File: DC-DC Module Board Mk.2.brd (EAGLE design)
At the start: 177.9 x 101.7 mm, 148 parts, among them U1 PCA9685, U3 LM1085IS-5.0

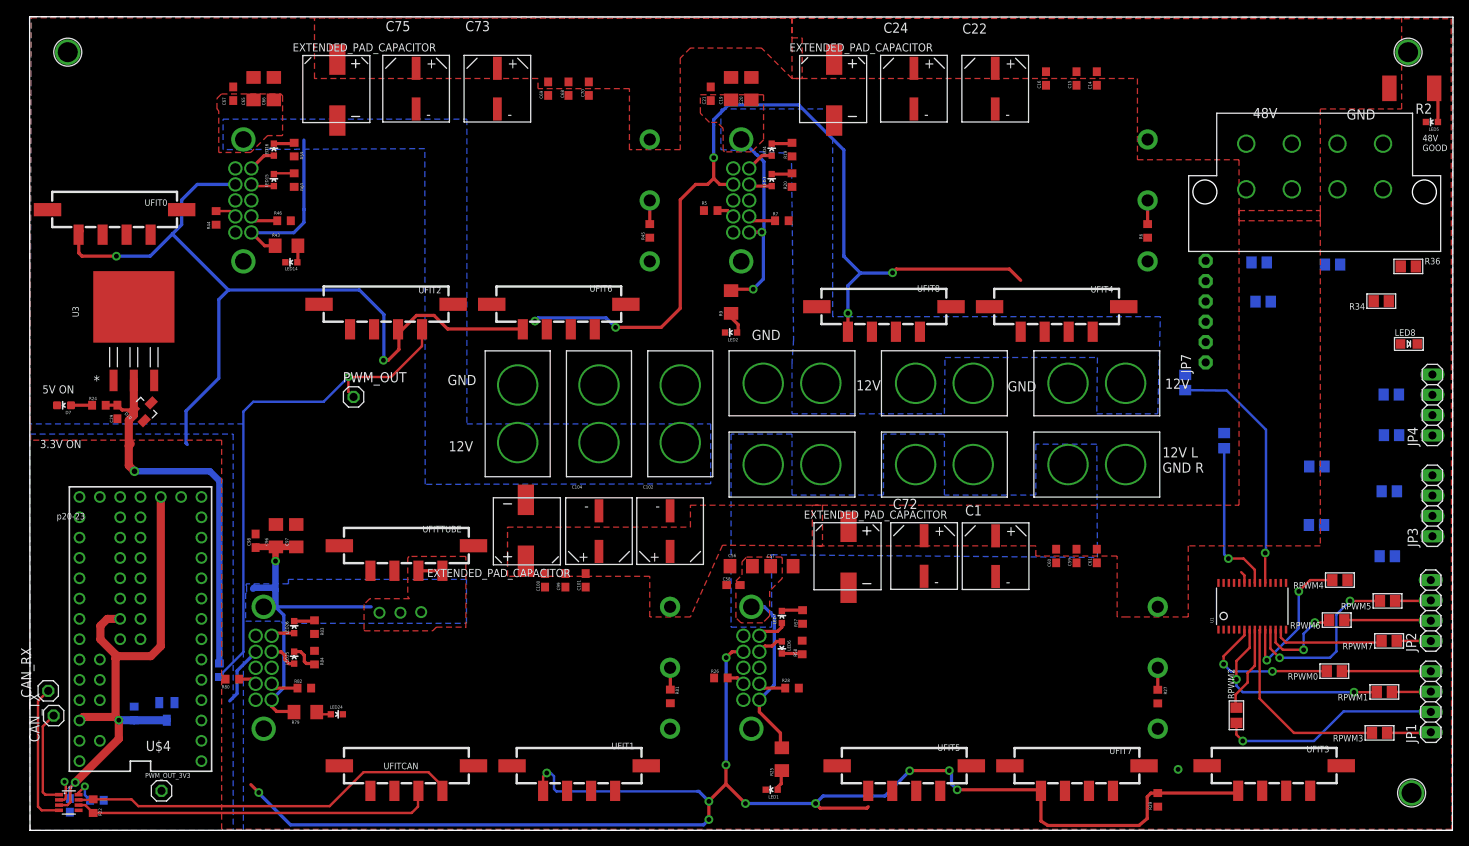
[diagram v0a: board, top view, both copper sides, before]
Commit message: pwm chip headers wired
need to give the bottom half more room so wires can come in
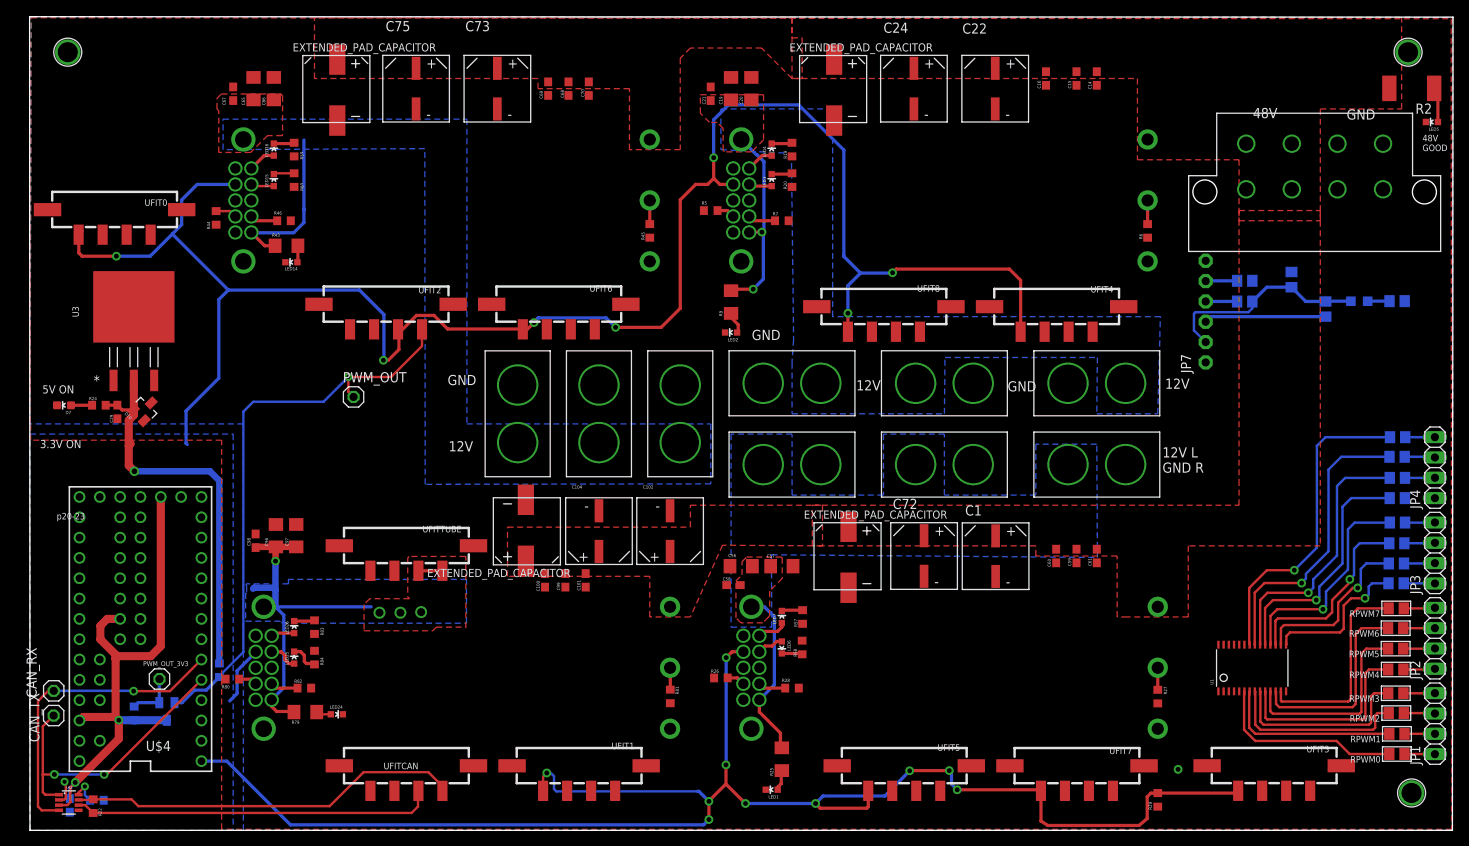
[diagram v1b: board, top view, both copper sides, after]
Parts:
- moved RPWM12 30.2 mm to (170.9, 40.3), turned to 0 degrees
- moved RPWM14 21.7 mm to (170.9, 45.4), turned to 0 degrees
- moved RPWM2 20.0 mm to (170.8, 13.4), turned to 180 degrees
- moved RPWM8 17.6 mm to (170.8, 29.6)
- moved PWM_OUT_3V3 14.0 mm to (16.2, 17.6)
- moved RPWM4 13.2 mm to (170.7, 18.8)
- moved RPWM0 13.0 mm to (170.9, 8.27)
- moved RPWM13 10.4 mm to (170.9, 42.8)
- moved RPWM10 10.3 mm to (170.8, 34.6)
- moved RPWM9 9.06 mm to (170.8, 32.1)
- moved LED8 8.18 mm to (166.2, 64.9), flipped to the bottom, turned to 90 degrees
- moved JP4 7.84 mm to (175.6, 44.1)
- moved U1 7.72 mm to (152.8, 19.0)
- moved RPWM6 7.44 mm to (170.7, 24.0)
- moved R34 7.06 mm to (161.9, 63.9), flipped to the bottom, turned to 90 degrees
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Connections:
- net DGND: now also UFIT4.C1, UFIT5.C1, UFIT6.C1
- net N$14: now also JP2.3; no longer JP2.2
- net N$20: now also JP2.4; no longer JP2.1
- net N$21: now also JP2.2; no longer JP2.3
- net N$24: now also JP2.1; no longer JP2.4
- net N$26: now also JP1.4; no longer JP1.1
- net N$27: now also JP1.3; no longer JP1.2
- net N$28: now also JP1.2; no longer JP1.3
- net N$29: now also JP1.1; no longer JP1.4
- net N$30: now also JP3.1; no longer JP3.4
- net N$31: now also JP3.2; no longer JP3.3
- net N$32: now also JP3.3; no longer JP3.2
- net N$37: now also JP3.4; no longer JP3.1
- net N$38: now also JP4.1; no longer JP4.4
- net N$39: now also JP4.2; no longer JP4.3
- net N$40: now also JP4.3; no longer JP4.2
- net N$41: now also JP4.4; no longer JP4.1
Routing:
- net PWM15: track 0.00 -> 40.0 mm, vias 0 -> 1
- net PWM13: track 0.00 -> 33.8 mm, vias 0 -> 1
- net PWM11: track 0.00 -> 27.4 mm, vias 0 -> 1
- net VCC: track 0.00 -> 26.4 mm
- net TXD: track 12.3 -> 37.0 mm, vias 0 -> 2
- net PWM10: track 0.00 -> 24.3 mm, vias 0 -> 1
- net N$27: track 27.7 -> 3.90 mm, vias 1 -> 0
- net PWM9: track 0.00 -> 21.4 mm, vias 0 -> 1
- net RXD: track 17.8 -> 38.6 mm, vias 0 -> 1
- net PWM8: track 0.00 -> 18.9 mm, vias 0 -> 1
- net DGND: track 424.3 -> 442.0 mm, vias 19 -> 18
- net PWM14: track 19.5 -> 36.7 mm
- net SDA: track 0.00 -> 15.2 mm
- net PWM6: track 11.4 -> 25.0 mm, vias 2 -> 0
- net PWM2: track 10.8 -> 22.9 mm
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
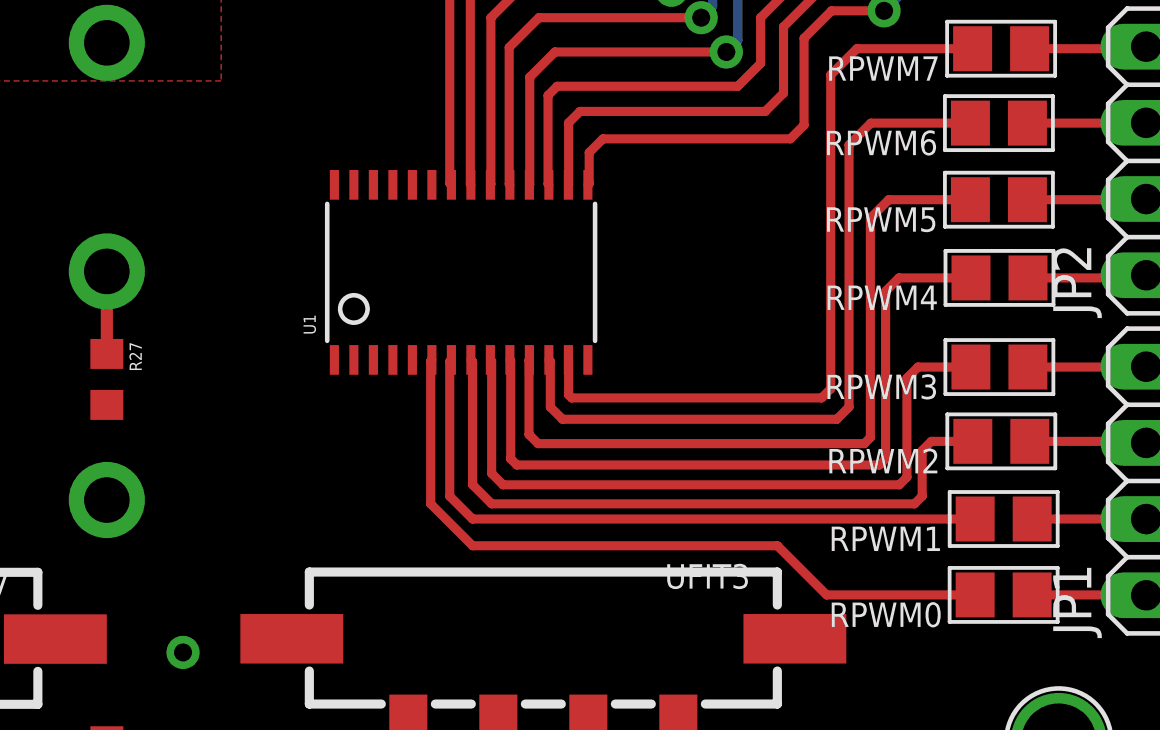
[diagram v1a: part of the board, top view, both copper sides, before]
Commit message: expanded space for other traces to reach pwm lines
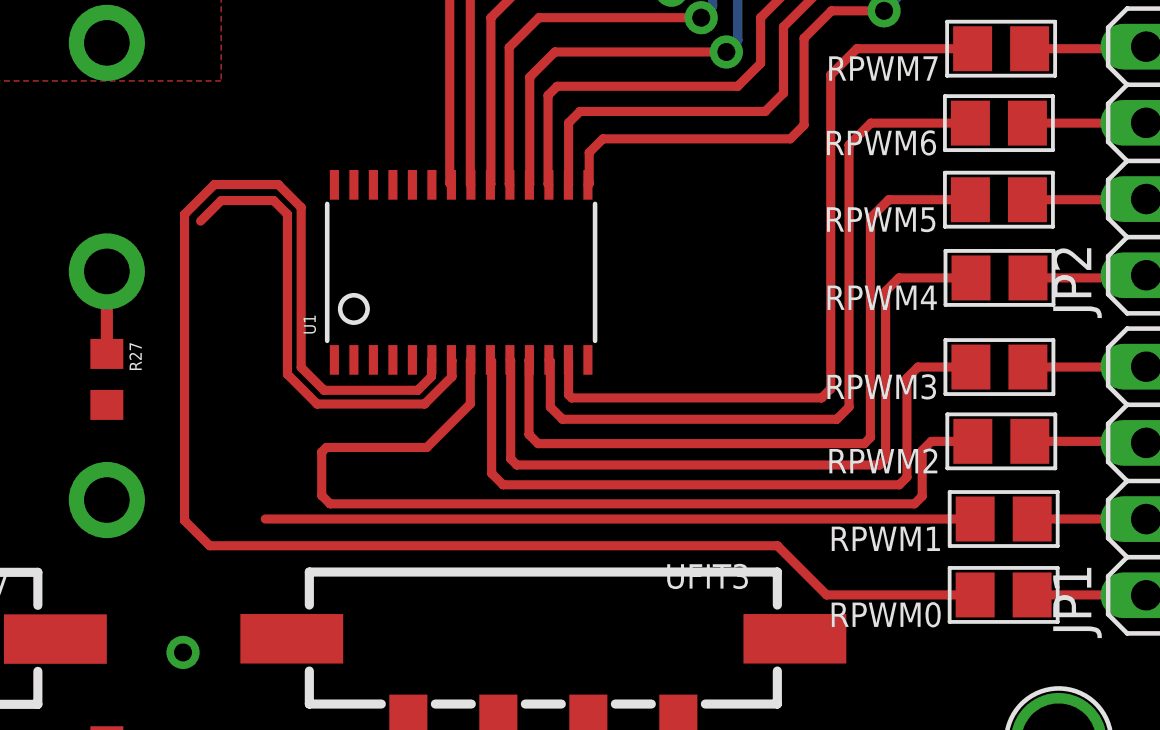
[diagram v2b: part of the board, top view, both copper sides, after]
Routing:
- net PWM0: track 24.2 -> 52.9 mm
- net PWM1: track 22.4 -> 39.2 mm
- net PWM2: track 22.9 -> 32.1 mm
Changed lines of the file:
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@@
 <contactref element="C22V4" pad="P$1"/>
 <wire x1="157.005" y1="16.1006" x2="150.505" y2="21.9362" width="0" layer="19" extent="1-1"/>
+<wire x1="140.97" y1="14.6" x2="150.505" y2="21.9362" width="0" layer="19" extent="1-1"/>
 </signal>
 <signal name="N$7">
@@
 <wire x1="169.9132" y1="8.2668" x2="164.9612" y2="8.2668" width="0.3048" layer="1"/>
 <wire x1="164.9612" y1="8.2668" x2="163.322" y2="9.906" width="0.3048" layer="1"/>
-<wire x1="163.322" y1="9.906" x2="153.162" y2="9.906" width="0.3048" layer="1"/>
-<wire x1="153.162" y1="9.906" x2="151.765" y2="11.303" width="0.3048" layer="1"/>
-<wire x1="151.765" y1="11.303" x2="151.765" y2="16.0606" width="0.3048" layer="1"/>
-<wire x1="151.765" y1="16.0606" x2="151.805" y2="16.1006" width="0.3048" layer="1"/>
+<wire x1="163.322" y1="9.906" x2="144.399" y2="9.906" width="0.3048" layer="1"/>
+<wire x1="144.399" y1="9.906" x2="143.5608" y2="10.7442" width="0.3048" layer="1"/>
+<wire x1="151.7904" y1="16.086" x2="151.805" y2="16.1006" width="0.3048" layer="1"/>
+<wire x1="143.5608" y1="10.7442" x2="143.5608" y2="20.955" width="0.3048" layer="1"/>
+<wire x1="143.5608" y1="20.955" x2="144.5514" y2="21.9456" width="0.3048" layer="1"/>
+<wire x1="144.5514" y1="21.9456" x2="146.685" y2="21.9456" width="0.3048" layer="1"/>
+<wire x1="146.685" y1="21.9456" x2="147.447" y2="21.1836" width="0.3048" layer="1"/>
+<wire x1="147.447" y1="21.1836" x2="147.447" y2="15.8496" width="0.3048" layer="1"/>
+<wire x1="147.447" y1="15.8496" x2="148.209" y2="15.0876" width="0.3048" layer="1"/>
+<wire x1="151.7904" y1="16.086" x2="151.7904" y2="15.5448" width="0.3048" layer="1"/>
+<wire x1="151.7904" y1="15.5448" x2="151.3332" y2="15.0876" width="0.3048" layer="1"/>
+<wire x1="151.3332" y1="15.0876" x2="148.209" y2="15.0876" width="0.3048" layer="1"/>
 </signal>
 <signal name="PWM1">
@@
 <contactref element="RPWM1" pad="2"/>
 <contactref element="UFIT1" pad="C4"/>
-<wire x1="169.9148" y1="10.7976" x2="153.1594" y2="10.7976" width="0.3048" layer="1"/>
-<wire x1="153.1594" y1="10.7976" x2="152.4" y2="11.557" width="0.3048" layer="1"/>
-<wire x1="152.4" y1="11.557" x2="152.4" y2="16.0456" width="0.3048" layer="1"/>
-<wire x1="152.4" y1="16.0456" x2="152.455" y2="16.1006" width="0.3048" layer="1"/>
-<wire x1="73.14" y1="3.665" x2="152.4" y2="11.557" width="0" layer="19" extent="1-1"/>
+<wire x1="169.9148" y1="10.7976" x2="146.2506" y2="10.7976" width="0.3048" layer="1"/>
+<wire x1="151.4094" y1="13.716" x2="152.4762" y2="14.7828" width="0" layer="19" extent="1-16"/>
+<wire x1="152.4762" y1="16.0794" x2="152.455" y2="16.1006" width="0.3048" layer="1"/>
+<wire x1="146.2506" y1="10.7976" x2="151.4094" y2="13.716" width="0" layer="19" extent="1-1"/>
+<wire x1="73.14" y1="3.665" x2="146.2506" y2="10.7976" width="0" layer="19" extent="1-1"/>
+<wire x1="152.4762" y1="16.0794" x2="152.4762" y2="15.5448" width="0.3048" layer="1"/>
+<wire x1="152.4762" y1="15.5448" x2="151.5618" y2="14.6304" width="0.3048" layer="1"/>
+<wire x1="151.5618" y1="14.6304" x2="147.9804" y2="14.6304" width="0.3048" layer="1"/>
+<wire x1="147.9804" y1="14.6304" x2="146.9898" y2="15.621" width="0.3048" layer="1"/>
+<wire x1="146.9898" y1="21.0312" x2="146.5326" y2="21.4884" width="0" layer="19" extent="1-16"/>
+<wire x1="146.5326" y1="21.4884" x2="146.2506" y2="10.7976" width="0" layer="19" extent="1-16"/>
+<wire x1="146.9898" y1="15.621" x2="146.9898" y2="20.955" width="0.3048" layer="1"/>
+<wire x1="146.9898" y1="20.955" x2="146.5326" y2="21.4122" width="0.3048" layer="1"/>
+<wire x1="146.5326" y1="21.4122" x2="144.78" y2="21.4122" width="0.3048" layer="1"/>
+<wire x1="144.78" y1="21.4122" x2="144.0942" y2="20.7264" width="0.3048" layer="1"/>
+<wire x1="144.0942" y1="20.7264" x2="146.2506" y2="10.7976" width="0" layer="19" extent="1-16"/>
 </signal>
 <signal name="PWM2">
@@
 <wire x1="168.148" y1="13.081" x2="168.148" y2="11.557" width="0.3048" layer="1"/>
 <wire x1="168.148" y1="11.557" x2="167.894" y2="11.303" width="0.3048" layer="1"/>
-<wire x1="167.894" y1="11.303" x2="153.797" y2="11.303" width="0.3048" layer="1"/>
-<wire x1="153.797" y1="11.303" x2="153.162" y2="11.938" width="0.3048" layer="1"/>
-<wire x1="153.162" y1="11.938" x2="153.162" y2="16.0436" width="0.3048" layer="1"/>
-<wire x1="153.162" y1="16.0436" x2="153.105" y2="16.1006" width="0.3048" layer="1"/>
-<wire x1="15.0756" y1="73.1848" x2="153.105" y2="16.1006" width="0" layer="19" extent="1-1"/>
+<wire x1="167.894" y1="11.303" x2="148.4122" y2="11.303" width="0.3048" layer="1"/>
+<wire x1="148.4122" y1="11.303" x2="148.1328" y2="11.5824" width="0.3048" layer="1"/>
+<wire x1="148.1328" y1="11.5824" x2="148.1328" y2="13.0302" width="0.3048" layer="1"/>
+<wire x1="148.1328" y1="13.0302" x2="148.2852" y2="13.1826" width="0.3048" layer="1"/>
+<wire x1="148.2852" y1="13.1826" x2="151.638" y2="13.1826" width="0.3048" layer="1"/>
+<wire x1="151.638" y1="13.1826" x2="153.0858" y2="14.6304" width="0.3048" layer="1"/>
+<wire x1="153.0858" y1="14.6304" x2="153.0858" y2="16.0814" width="0.3048" layer="1"/>
+<wire x1="153.0858" y1="16.0814" x2="153.105" y2="16.1006" width="0.3048" layer="1"/>
+<wire x1="15.0756" y1="73.1848" x2="148.1328" y2="13.0302" width="0" layer="19" extent="1-1"/>
 </signal>
 <signal name="PWM3">

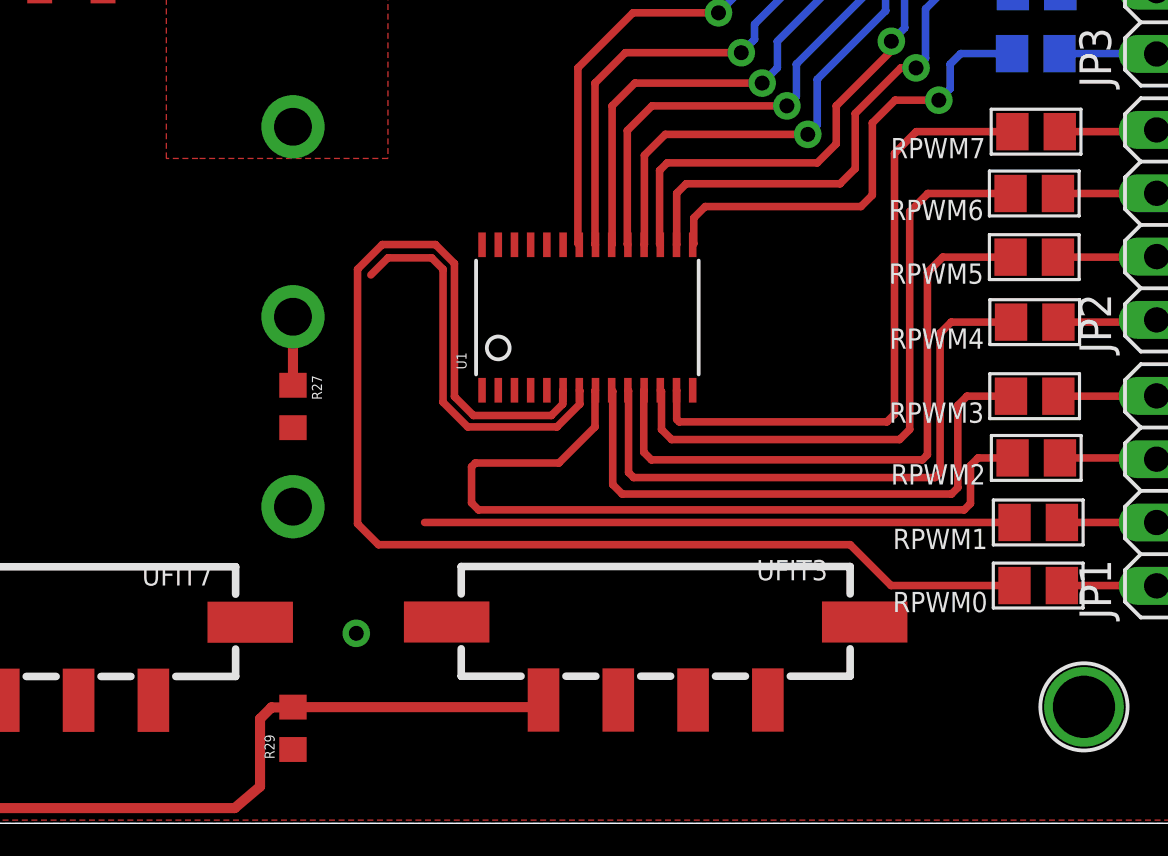
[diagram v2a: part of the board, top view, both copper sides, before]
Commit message: reorganized pwm chip layout
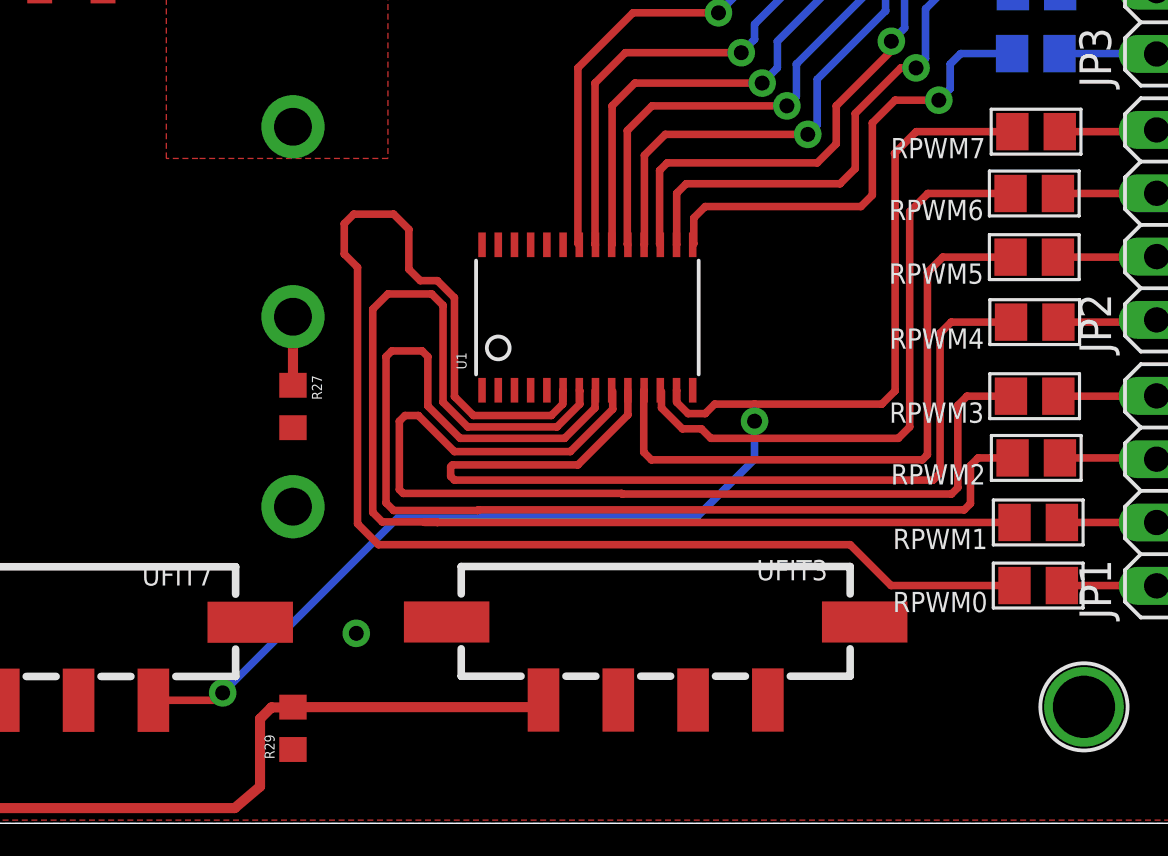
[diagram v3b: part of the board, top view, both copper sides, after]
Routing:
- net PWM7: track 25.6 -> 54.8 mm, vias 0 -> 2
- net PWM3: track 23.5 -> 41.6 mm
- net PWM4: track 24.6 -> 37.8 mm
- net PWM2: track 32.1 -> 45.2 mm
- net PWM1: track 39.2 -> 48.6 mm
- net PWM0: track 52.9 -> 55.9 mm
- net PWM6: track 25.0 -> 24.3 mm
